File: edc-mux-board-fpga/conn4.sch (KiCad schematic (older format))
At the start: 24 parts, among them U16 MAX4910, U17 TLV320AIC3206, U18 P82B96

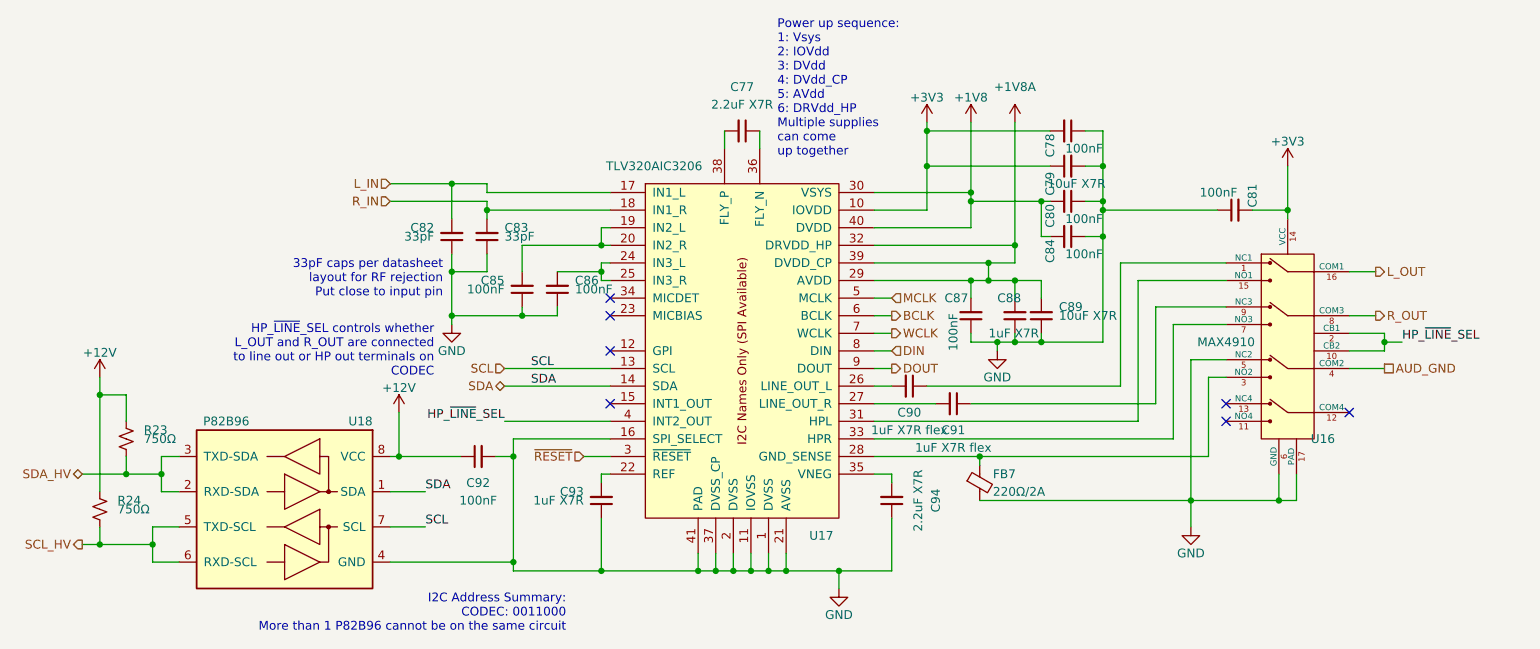
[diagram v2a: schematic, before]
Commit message: re-annotating after adding power ICs and decoupling capacitors.
Also verified most footprints, and updated schematic field data.
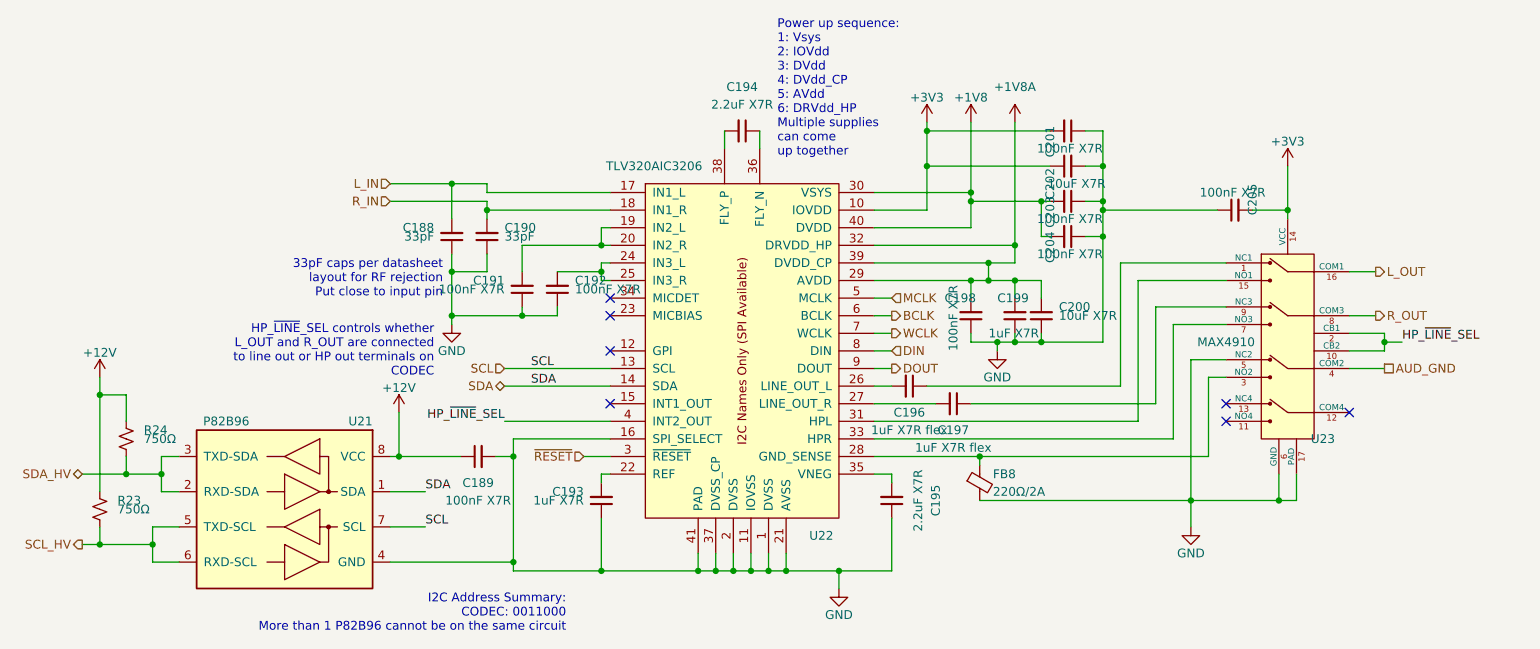
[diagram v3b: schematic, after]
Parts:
- C189: renamed from C92; value 100nF -> 100nF X7R
- C191: renamed from C85; value 100nF -> 100nF X7R
- C192: renamed from C86; value 100nF -> 100nF X7R
- C198: renamed from C87; value 100nF -> 100nF X7R
- C201: renamed from C78; value 100nF -> 100nF X7R
- C203: renamed from C80; value 100nF -> 100nF X7R
- C204: renamed from C84; value 100nF -> 100nF X7R
- C205: renamed from C81; value 100nF -> 100nF X7R
- R23: renamed from R24; Package ID (none) -> 0402in/1005mm
- R24: renamed from R23; Package ID (none) -> 0402in/1005mm
- renumbered C82 to C188, C83 to C190, C93 to C193, C77 to C194, C94 to C195, C90 to C196, C91 to C197, C88 to C199, C89 to C200, C79 to C202, FB7 to FB8, U18 to U21, U17 to U22, U16 to U23

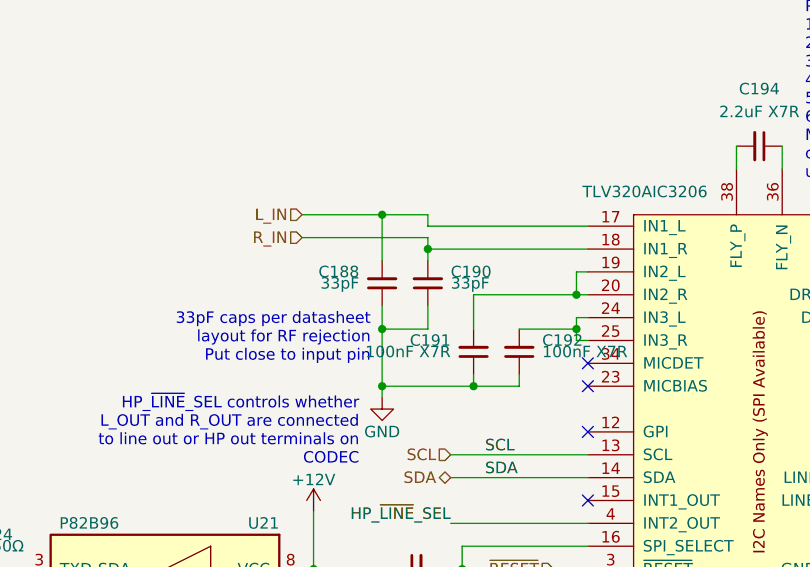
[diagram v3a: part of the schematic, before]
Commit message: Reannotating and adding more fields to components
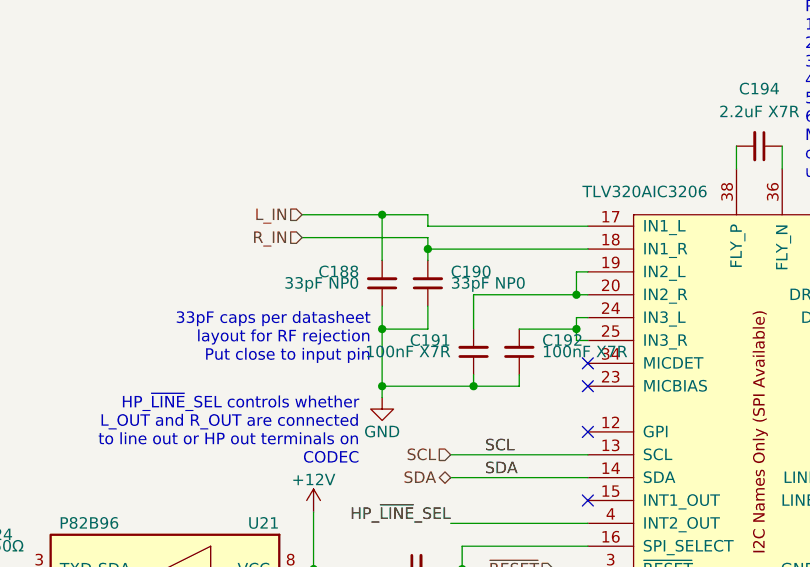
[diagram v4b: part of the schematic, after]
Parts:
- C188, C190: value 33pF -> 33pF NP0; footprint Capacitor_SMD:C_0603_1608Metric -> Capacitor_SMD:C_0402_1005Metric; Characteristics (none) -> CAP CER 33PF 25V NP0 0402; Description (none) -> MLCC Capacitor; Manufacturer (none) -> AVX; Manufacturers Part Number (none) -> 04023A330FAT2A; Package ID 0603in/1608mm -> 0402in/1005mm
- C189, C191, C192, C198, C201, C203, C204, C205: Characteristics (none) -> CAP CER 0.1UF 25V X7R 0603; Description (none) -> MLCC Capacitor; Manufacturer (none) -> Kemet; Manufacturers Part Number (none) -> C0603C104J3RACAUTO
- C193, C199: Characteristics (none) -> CAP CER 1UF 25V X7R 0603; Description (none) -> MLCC Capacitor
- C194, C195: footprint Capacitor_SMD:C_0603_1608Metric -> Capacitor_SMD:C_0805_2012Metric; Characteristics (none) -> CAP CER 2.2UF 25V X7R 0805; Description (none) -> MLCC Capacitor; Manufacturer (none) -> TDK; Manufacturers Part Number (none) -> CGA4J3X7R1E225K125AB; Package ID 0603in/1608mm -> 0805in/2012mm
- C196, C197: Characteristics (none) -> CAP CER 0805 1UF 25V X7R 5%; Description (none) -> MLCC Capacitor; Manufacturers Part Number C0805X105J3RACAUTO -> C0805X105J3RECAUTO
- C200, C202: Characteristics (none) -> CAP CER 10UF 25V X7R 1206; Description (none) -> MLCC Capacitor
- FB8: footprint Resistor_SMD:R_0603_1608Metric -> Inductor_SMD:L_0603_1608Metric; Description (none) -> Ferrite Bead
- R23, R24: Description (none) -> Resistor
- U21: Description (none) -> I2C Buffer / Voltage Translator; Manufacturer (none) -> Texas Instruments; Manufacturers Part Number (none) -> P82B96; Package ID (none) -> TSSOP8
- U22: Description (none) -> I2S Audio Codec; Manufacturer (none) -> Texas Instruments; Package ID (none) -> UQFN40
- U23: Description (none) -> Clickless Audio Switch; Manufacturer (none) -> Maxim Integrated; Package ID (none) -> TQFN16

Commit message: Fixed resistor footprint
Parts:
- R23, R24: footprint Resistor_SMD:R_0603_1608Metric -> Resistor_SMD:R_0402_1005Metric
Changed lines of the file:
@@
 F 0 "R24" H 1800 3950 50  0000 L CNN
 F 1 "750Ω" H 1800 3900 50  0000 L CNN
-F 2 "Resistor_SMD:R_0603_1608Metric" H 1700 3900 50  0001 C CNN
+F 2 "Resistor_SMD:R_0402_1005Metric" H 1700 3900 50  0001 C CNN
 F 3 "~" H 1700 3900 50  0001 C CNN
 F 4 "0402in/1005mm" H 0   0   50  0001 C CNN "Package ID"
@@
 F 0 "R23" H 1650 4350 50  0000 L CNN
 F 1 "750Ω" H 1650 4300 50  0000 L CNN
-F 2 "Resistor_SMD:R_0603_1608Metric" H 1550 4300 50  0001 C CNN
+F 2 "Resistor_SMD:R_0402_1005Metric" H 1550 4300 50  0001 C CNN
 F 3 "~" H 1550 4300 50  0001 C CNN
 F 4 "0402in/1005mm" H 0   0   50  0001 C CNN "Package ID"
